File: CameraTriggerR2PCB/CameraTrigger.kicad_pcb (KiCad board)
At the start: 2 copper layers, 99.1 x 99.1 mm, 51 parts, among them J1 Power, J10 feather short, J11 Ada2633, J12 Camera 2.5mm, J2 Camera 3.5mm, J3 Aux out, J4 HighLowIn, J5 Laser, J6 Sensor, J7 Trig, J8 Arm, J9 Ada3178, Q1 PN2222A, Q2 PN2222A, Q3 PN2222A, SW1 SW_Power, SW2 SW_Trigger, SW3 SW_Poll, SW4 SW_Arm, U1 LM7805_TO220, U2 ILD74, U3 ILD74

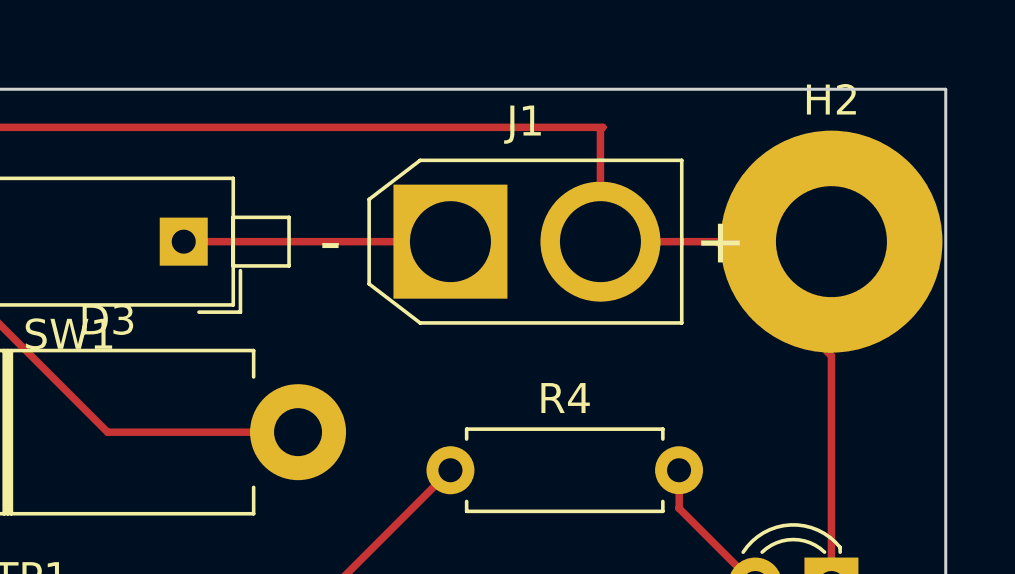
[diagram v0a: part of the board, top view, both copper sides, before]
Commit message: Add files via upload
Fixes on R2 board
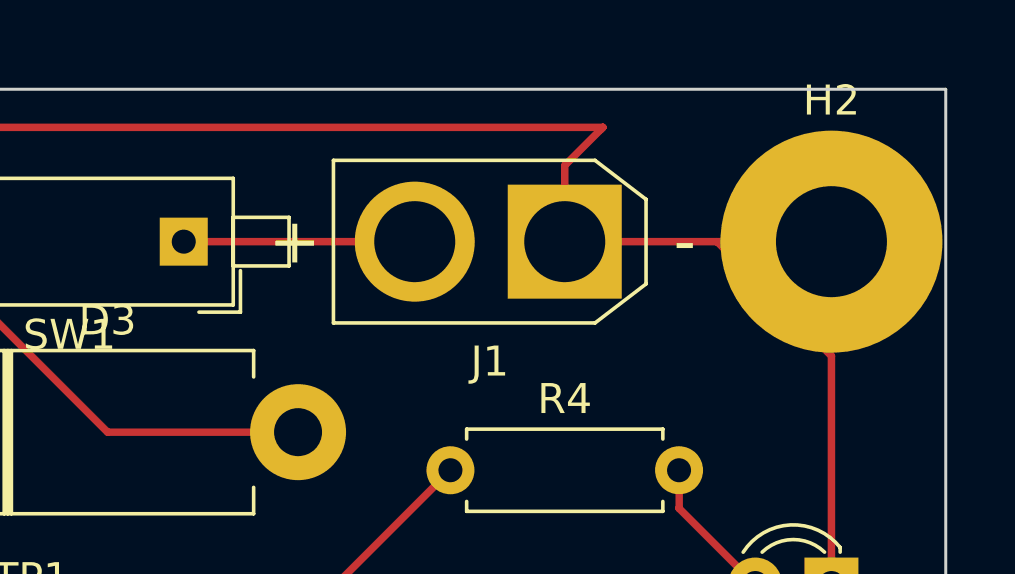
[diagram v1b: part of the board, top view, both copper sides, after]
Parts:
- J1: footprint Connector_AMASS:AMASS_XT30U-F_1x02_P5.0mm_Vertical -> AMASS_XT30U-F_1x02_P5.0mm_Vertical
- moved J1 3.81 mm to (99.1, 17.8), turned to 180 degrees
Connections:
- J1 pad 1: +7.5V -> GND
- J1 pad 2: GND -> +7.5V
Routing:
- net GND: track 495.5 -> 497.3 mm
- net +7.5V: track 8.89 -> 7.70 mm
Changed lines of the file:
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@@
     (thickness 1.6)
     (drawings 5)
-    (tracks 309)
+    (tracks 310)
     (zones 0)
     (modules 51)
@@
     )
   )
-  (module Connector_AMASS:AMASS_XT30U-F_1x02_P5.0mm_Vertical (layer F.Cu)
-    (at 95.25 17.78)
-    (descr "Connector XT30 Vertical Cable Female, https://www.tme.eu/en/Document/3cbfa5cfa544d79584972dd5234a409e/XT30U%20SPEC.pdf")
-    (tags "RC Connector XT30")
-    (fp_text reference J1 (at 2.5 -4) (layer F.SilkS)
-      (effects (font (size 1 1) (thickness 0.15)))
-    )
-    (fp_text value Power (at 2.5 4) (layer F.Fab)
-      (effects (font (size 1 1) (thickness 0.15)))
-    )
-    (fp_text user - (at -4 0) (layer F.SilkS)
-      (effects (font (size 1.5 1.5) (thickness 0.15)))
-    )
-    (fp_text user + (at 9 0) (layer F.SilkS)
-      (effects (font (size 1.5 1.5) (thickness 0.15)))
-    )
-    (fp_line (start -3.1 1.8) (end -1.4 3.1) (layer F.CrtYd) (width 0.05))
-    (fp_line (start -3.1 -1.8) (end -1.4 -3.1) (layer F.CrtYd) (width 0.05))
-    (fp_line (start -1.4 3.1) (end 8.1 3.1) (layer F.CrtYd) (width 0.05))
-    (fp_line (start -3.1 -1.8) (end -3.1 1.8) (layer F.CrtYd) (width 0.05))
-    (fp_line (start 8.1 -3.1) (end 8.1 3.1) (layer F.CrtYd) (width 0.05))
-    (fp_line (start -1.4 -3.1) (end 8.1 -3.1) (layer F.CrtYd) (width 0.05))
-    (fp_line (start -2.71 -1.41) (end -2.71 1.41) (layer F.SilkS) (width 0.12))
-    (fp_line (start -2.71 1.41) (end -1.01 2.71) (layer F.SilkS) (width 0.12))
-    (fp_line (start -2.71 -1.41) (end -1.01 -2.71) (layer F.SilkS) (width 0.12))
-    (fp_line (start -1.01 2.71) (end 7.71 2.71) (layer F.SilkS) (width 0.12))
-    (fp_line (start 7.71 -2.71) (end 7.71 2.71) (layer F.SilkS) (width 0.12))
-    (fp_line (start -1.01 -2.71) (end 7.71 -2.71) (layer F.SilkS) (width 0.12))
-    (fp_line (start -2.6 1.3) (end -0.9 2.6) (layer F.Fab) (width 0.1))
-    (fp_line (start -2.6 -1.3) (end -0.9 -2.6) (layer F.Fab) (width 0.1))
-    (fp_line (start -0.9 2.6) (end 7.6 2.6) (layer F.Fab) (width 0.1))
-    (fp_line (start -0.9 -2.6) (end 7.6 -2.6) (layer F.Fab) (width 0.1))
-    (fp_line (start 7.6 -2.6) (end 7.6 2.6) (layer F.Fab) (width 0.1))
-    (fp_line (start -2.6 -1.3) (end -2.6 1.3) (layer F.Fab) (width 0.1))
-    (fp_text user %R (at 2.5 0) (layer F.Fab)
-      (effects (font (size 1 1) (thickness 0.15)))
-    )
-    (pad 2 thru_hole circle (at 5 0) (size 4 4) (drill 2.7) (layers *.Cu *.Mask)
-      (net 1 GND))
-    (pad 1 thru_hole rect (at 0 0) (size 3.8 3.8) (drill 2.7) (layers *.Cu *.Mask)
-      (net 13 +7.5V))
-    (model ${KISYS3DMOD}/Connector_AMASS.3dshapes/AMASS_XT30U-F_1x02_P5.0mm_Vertical.wrl
-      (at (xyz 0 0 0))
-      (scale (xyz 1 1 1))
-      (rotate (xyz 0 0 0))
-    )
-  )
   (module Package_DIP:DIP-8_W7.62mm (layer F.Cu)
     (at 95.25 41.91)
@@
       (net 2 Buzzer))
     (model ${KISYS3DMOD}/Buzzer_Beeper.3dshapes/Buzzer_TDK_PS1240P02BT_D12.2mm_H6.5mm.wrl
+      (at (xyz 0 0 0))
+      (scale (xyz 1 1 1))
+      (rotate (xyz 0 0 0))
+    )
+  )
+  (module AMASS_XT30U-F_1x02_P5.0mm_Vertical (layer F.Cu)
+    (at 99.06 17.78 180)
+    (descr "Connector XT30 Vertical Cable Female, https://www.tme.eu/en/Document/3cbfa5cfa544d79584972dd5234a409e/XT30U%20SPEC.pdf")
+    (tags "RC Connector XT30")
+    (fp_text reference J1 (at 2.5 -4) (layer F.SilkS)
+      (effects (font (size 1 1) (thickness 0.15)))
+    )
+    (fp_text value Power (at 2.5 4) (layer F.Fab)
+      (effects (font (size 1 1) (thickness 0.15)))
+    )
+    (fp_line (start -2.6 -1.3) (end -2.6 1.3) (layer F.Fab) (width 0.1))
+    (fp_line (start 7.6 -2.6) (end 7.6 2.6) (layer F.Fab) (width 0.1))
+    (fp_line (start -0.9 -2.6) (end 7.6 -2.6) (layer F.Fab) (width 0.1))
+    (fp_line (start -0.9 2.6) (end 7.6 2.6) (layer F.Fab) (width 0.1))
+    (fp_line (start -2.6 -1.3) (end -0.9 -2.6) (layer F.Fab) (width 0.1))
+    (fp_line (start -2.6 1.3) (end -0.9 2.6) (layer F.Fab) (width 0.1))
+    (fp_line (start -1.01 -2.71) (end 7.71 -2.71) (layer F.SilkS) (width 0.12))
+    (fp_line (start 7.71 -2.71) (end 7.71 2.71) (layer F.SilkS) (width 0.12))
+    (fp_line (start -1.01 2.71) (end 7.71 2.71) (layer F.SilkS) (width 0.12))
+    (fp_line (start -2.71 -1.41) (end -1.01 -2.71) (layer F.SilkS) (width 0.12))
+    (fp_line (start -2.71 1.41) (end -1.01 2.71) (layer F.SilkS) (width 0.12))
+    (fp_line (start -2.71 -1.41) (end -2.71 1.41) (layer F.SilkS) (width 0.12))
+    (fp_line (start -1.4 -3.1) (end 8.1 -3.1) (layer F.CrtYd) (width 0.05))
+    (fp_line (start 8.1 -3.1) (end 8.1 3.1) (layer F.CrtYd) (width 0.05))
+    (fp_line (start -3.1 -1.8) (end -3.1 1.8) (layer F.CrtYd) (width 0.05))
+    (fp_line (start -1.4 3.1) (end 8.1 3.1) (layer F.CrtYd) (width 0.05))
+    (fp_line (start -3.1 -1.8) (end -1.4 -3.1) (layer F.CrtYd) (width 0.05))
+    (fp_line (start -3.1 1.8) (end -1.4 3.1) (layer F.CrtYd) (width 0.05))
+    (fp_text user + (at 9 0) (layer F.SilkS)
+      (effects (font (size 1.5 1.5) (thickness 0.15)))
+    )
+    (fp_text user - (at -4 0) (layer F.SilkS)
+      (effects (font (size 1.5 1.5) (thickness 0.15)))
+    )
+    (pad 1 thru_hole rect (at 0 0 180) (size 3.8 3.8) (drill 2.7) (layers *.Cu *.Mask)
+      (net 1 GND))
+    (pad 2 thru_hole circle (at 5 0 180) (size 4 4) (drill 2.7) (layers *.Cu *.Mask)
+      (net 13 +7.5V))
+    (model ${KISYS3DMOD}/Connector_AMASS.3dshapes/AMASS_XT30U-F_1x02_P5.0mm_Vertical.wrl
       (at (xyz 0 0 0))
       (scale (xyz 1 1 1))
@@
   (segment (start 85.09 44.45) (end 85.09 39.37) (width 0.25) (layer B.Cu) (net 1))
   (segment (start 85.09 39.37) (end 87.63 39.37) (width 0.25) (layer B.Cu) (net 1))
-  (segment (start 100.25 14.05) (end 100.25 17.78) (width 0.25) (layer F.Cu) (net 1))
   (segment (start 100.33 13.97) (end 100.25 14.05) (width 0.25) (layer F.Cu) (net 1))
   (segment (start 71.12 20.32) (end 71.12 17.78) (width 0.25) (layer F.Cu) (net 1))
@@
   (segment (start 67.31 24.13) (end 71.12 20.32) (width 0.25) (layer F.Cu) (net 1))
   (segment (start 69.85 13.97) (end 100.33 13.97) (width 0.25) (layer F.Cu) (net 1))
-  (segment (start 100.25 17.78) (end 107.95 17.78) (width 0.25) (layer F.Cu) (net 1))
+  (segment (start 99.06 17.78) (end 107.95 17.78) (width 0.25) (layer F.Cu) (net 1))
+  (segment (start 99.06 15.24) (end 99.06 17.78) (width 0.25) (layer F.Cu) (net 1))
+  (segment (start 100.33 13.97) (end 99.06 15.24) (width 0.25) (layer F.Cu) (net 1))
   (segment (start 59.69 48.26) (end 55.88 48.26) (width 0.25) (layer F.Cu) (net 2))
   (segment (start 52.07 52.07) (end 52.07 73.66) (width 0.25) (layer F.Cu) (net 2))
@@
   (segment (start 59.69 45.72) (end 63.5 45.72) (width 0.25) (layer F.Cu) (net 11))
   (segment (start 68.58 48.26) (end 74.93 48.26) (width 0.25) (layer F.Cu) (net 12))
-  (segment (start 86.36 17.78) (end 95.25 17.78) (width 0.25) (layer F.Cu) (net 13))
+  (segment (start 86.36 17.78) (end 94.06 17.78) (width 0.25) (layer F.Cu) (net 13))
   (segment (start 80.55 61.69) (end 73.66 68.58) (width 0.25) (layer B.Cu) (net 14))
   (segment (start 98.78 61.69) (end 80.55 61.69) (width 0.25) (layer B.Cu) (net 14))

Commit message: Rev2B changes
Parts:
- added GND1: TestPoint, TestPoint:TestPoint_Keystone_5000-5004_Miniature, F.Cu at (30.5, 17.8)
- added H5: MountingHole, MountingHole:MountingHole_4.5mm, F.Cu at (38.1, 71.1)
- added J13: +5V Always on, TerminalBlock_TE-Connectivity:TerminalBlock_TE_282834-2_1x02_P2.54mm_Horizontal, F.Cu at (88.9, 81.3)
- added J14: Ext power switch, TerminalBlock_TE-Connectivity:TerminalBlock_TE_282834-2_1x02_P2.54mm_Horizontal, F.Cu at (81.3, 21.6)
- J1: footprint AMASS_XT30U-F_1x02_P5.0mm_Vertical -> Connector_AMASS:AMASS_XT30U-F_1x02_P5.0mm_Vertical
- J12: footprint CameraTriggerPCB:CUI_SJ1-3533NG -> CameraTriggerPCB:CUI_SJ1-2503A
- SW1: footprint Button_Switch_THT:SW_DIP_SPSTx01_Piano_10.8x4.1mm_W7.62mm_P2.54mm -> Button_Switch_THT:SW_DIP_SPSTx01_Slide_6.7x4.1mm_W7.62mm_P2.54mm_LowProfile
- moved TP9 18.3 mm to (58.4, 85.1)
- moved TP7Poll1 15.7 mm to (20.3, 47.0)
- moved R8 13.7 mm to (83.8, 96.5)
- moved J11 8.89 mm to (39.4, 87.6)
- moved J6 8.89 mm to (72.4, 97.8)
- moved SW1 8.03 mm to (78.7, 15.2)
- moved H1 8.03 mm to (106.7, 97.8)
- moved TP2+3.3V1 7.62 mm to (61.0, 99.1)
- moved H4 7.62 mm to (17.8, 97.8)
- moved D3 5.68 mm to (74.9, 29.2)
- moved D1 3.81 mm to (83.8, 91.4)
- moved J5 2.84 mm to (100.3, 92.7)
- moved J9 2.84 mm to (39.4, 59.7)
- moved TP1+5 2.84 mm to (80.0, 34.3)
- moved Q1 2.54 mm to (91.4, 91.4)
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- renumbered TP1 to TP1+5, TP2 to TP2+3.3V1, TP3 to TP3Arm1, TP4 to TP4Fire1, TP5 to TP5Trigger1, TP6 to TP6Arm1, TP7 to TP7Poll1
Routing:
- net GND: track 497.3 -> 791.7 mm
- net Net-(J12-PadR): track 30.3 -> 66.6 mm
- net +5V: track 242.3 -> 219.8 mm
- net +7.5V: track 7.70 -> 22.3 mm
- net +3V3: track 164.3 -> 151.4 mm
- net SCK: track 59.3 -> 71.3 mm
- net SensorIn: track 83.0 -> 71.2 mm
- net CS: track 55.6 -> 46.3 mm
- net Net-(D3-Pad2): track 14.8 -> 23.3 mm
- net MISO: track 50.7 -> 42.6 mm
- net Poll: track 20.4 -> 27.3 mm
- net MOSI: track 54.1 -> 48.3 mm
- net IRQ: track 59.3 -> 64.6 mm
- net ArmInd: track 45.9 -> 43.4 mm
- net Net-(J12-PadT): track 53.0 -> 55.1 mm
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- added copper zone on B.Cu, net GND
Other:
- board size 99.1 x 99.1 mm -> 99.1 x 90.2 mm
- board text added: "+5"
- board text added: "+5V, G"
- board text added: "Adafruit 2633"
- board text added: "Adafruit 3176 or 3178"
- board text added: "Arm"
- board text added: "Aux out +, G"
- board text added: "Heisey RocketTrig Rev2B"
- board text added: "HighLowSensor G, Sen, +3.3"
- board text added: "Laser out +, G"
- board text added: "LowHighSensor G, Sen, +3.3"
- board text added: "Poll"
- board text added: "SCK"
- board text added: "Trig"
